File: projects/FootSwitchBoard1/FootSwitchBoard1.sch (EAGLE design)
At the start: 10 parts

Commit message: Board updates.
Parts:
- added BD_V+, BD_V/2, GND, GND1, GND2, GND3, GND4, GND5, JK_V+: WIREPAD2,54/0,8, wirepad:WIREPAD2,54/0,8
- added C2: (no value), gm-caps-film-box:072X0352
- added C3: (no value), gm-caps-electro-pol:080
- added R3, R4: (no value), gm-resistors:6MM.4
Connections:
- new net N$10: BD_V/2.P, C3.+, R3.1, R4.2
- new net N$11: C1.-, C2.2, C3.-, GND.P, GND1.P, GND2.P, GND3.P, GND4.P, GND5.P, R4.1, U$1.A1, U$1.A2, U$1.B1
- new net N$9: BD_V+.P, C1.+, C2.1, D1.A, R2.2, R3.2
- net N$7: now also D2.A, JK_V+.P; no longer U$1.A1, U$1.A2, U$1.B1
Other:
- moved on the sheet: R2
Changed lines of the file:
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@@
 <part name="R2" library="gm-resistors" deviceset="6MM" device=".4"/>
 <part name="C1" library="gm-caps-electro-pol" deviceset="080" device=""/>
+<part name="C2" library="gm-caps-film-box" deviceset="072X035" device="2"/>
+<part name="R3" library="gm-resistors" deviceset="6MM" device=".4"/>
+<part name="R4" library="gm-resistors" deviceset="6MM" device=".4"/>
+<part name="C3" library="gm-caps-electro-pol" deviceset="080" device=""/>
+<part name="JK_V+" library="wirepad" deviceset="WIREPAD" device="2,54/0,8"/>
+<part name="GND" library="wirepad" deviceset="WIREPAD" device="2,54/0,8"/>
+<part name="BD_V/2" library="wirepad" deviceset="WIREPAD" device="2,54/0,8"/>
+<part name="BD_V+" library="wirepad" deviceset="WIREPAD" device="2,54/0,8"/>
+<part name="GND1" library="wirepad" deviceset="WIREPAD" device="2,54/0,8"/>
+<part name="GND2" library="wirepad" deviceset="WIREPAD" device="2,54/0,8"/>
+<part name="GND3" library="wirepad" deviceset="WIREPAD" device="2,54/0,8"/>
+<part name="GND4" library="wirepad" deviceset="WIREPAD" device="2,54/0,8"/>
+<part name="GND5" library="wirepad" deviceset="WIREPAD" device="2,54/0,8"/>
 </parts>
 <sheets>
@@
 <instance part="R1" gate="G$1" x="93.98" y="68.58"/>
 <instance part="D2" gate="1" x="17.78" y="81.28"/>
-<instance part="R2" gate="G$1" x="35.56" y="81.28"/>
+<instance part="R2" gate="G$1" x="30.48" y="81.28"/>
 <instance part="C1" gate="G$1" x="45.72" y="78.74"/>
+<instance part="C2" gate="G$1" x="53.34" y="76.2"/>
+<instance part="R3" gate="G$1" x="30.48" y="66.04" rot="R90"/>
+<instance part="R4" gate="G$1" x="30.48" y="50.8" rot="R90"/>
+<instance part="C3" gate="G$1" x="22.86" y="53.34"/>
+<instance part="JK_V+" gate="G$1" x="2.54" y="81.28"/>
+<instance part="GND" gate="G$1" x="5.08" y="45.72"/>
+<instance part="BD_V/2" gate="G$1" x="15.24" y="55.88"/>
+<instance part="BD_V+" gate="G$1" x="15.24" y="71.12"/>
+<instance part="GND1" gate="G$1" x="5.08" y="38.1"/>
+<instance part="GND2" gate="G$1" x="5.08" y="30.48"/>
+<instance part="GND3" gate="G$1" x="5.08" y="22.86"/>
+<instance part="GND4" gate="G$1" x="5.08" y="15.24"/>
+<instance part="GND5" gate="G$1" x="5.08" y="7.62"/>
 </instances>
 <busses>
@@
 </segment>
 </net>
-<net name="N$7" class="0">
-<segment>
+<net name="N$8" class="0">
+<segment>
+<pinref part="D2" gate="1" pin="C"/>
+<wire x1="20.32" y1="81.28" x2="25.4" y2="81.28" width="0.1524" layer="91"/>
+<pinref part="R2" gate="G$1" pin="1"/>
+</segment>
+</net>
+<net name="N$9" class="0">
+<segment>
+<pinref part="R2" gate="G$1" pin="2"/>
+<pinref part="C1" gate="G$1" pin="+"/>
+<wire x1="35.56" y1="81.28" x2="45.72" y2="81.28" width="0.1524" layer="91"/>
+<pinref part="C2" gate="G$1" pin="1"/>
+<wire x1="45.72" y1="81.28" x2="53.34" y2="81.28" width="0.1524" layer="91"/>
+<junction x="45.72" y="81.28"/>
+<wire x1="35.56" y1="81.28" x2="35.56" y2="73.66" width="0.1524" layer="91"/>
+<junction x="35.56" y="81.28"/>
+<pinref part="R3" gate="G$1" pin="2"/>
+<wire x1="35.56" y1="73.66" x2="30.48" y2="73.66" width="0.1524" layer="91"/>
+<wire x1="30.48" y1="73.66" x2="30.48" y2="71.12" width="0.1524" layer="91"/>
+<pinref part="D1" gate="G$1" pin="A"/>
+<wire x1="119.38" y1="68.58" x2="119.38" y2="78.74" width="0.1524" layer="91"/>
+<wire x1="119.38" y1="78.74" x2="60.96" y2="78.74" width="0.1524" layer="91"/>
+<wire x1="60.96" y1="78.74" x2="60.96" y2="81.28" width="0.1524" layer="91"/>
+<wire x1="60.96" y1="81.28" x2="53.34" y2="81.28" width="0.1524" layer="91"/>
+<junction x="53.34" y="81.28"/>
+<pinref part="BD_V+" gate="G$1" pin="P"/>
+<wire x1="17.78" y1="71.12" x2="25.4" y2="71.12" width="0.1524" layer="91"/>
+<wire x1="25.4" y1="71.12" x2="25.4" y2="73.66" width="0.1524" layer="91"/>
+<wire x1="25.4" y1="73.66" x2="30.48" y2="73.66" width="0.1524" layer="91"/>
+<junction x="30.48" y="73.66"/>
+</segment>
+</net>
+<net name="N$10" class="0">
+<segment>
+<pinref part="R3" gate="G$1" pin="1"/>
+<pinref part="R4" gate="G$1" pin="2"/>
+<wire x1="30.48" y1="60.96" x2="30.48" y2="55.88" width="0.1524" layer="91"/>
+<pinref part="C3" gate="G$1" pin="+"/>
+<wire x1="22.86" y1="55.88" x2="30.48" y2="55.88" width="0.1524" layer="91"/>
+<junction x="30.48" y="55.88"/>
+<pinref part="BD_V/2" gate="G$1" pin="P"/>
+<wire x1="17.78" y1="55.88" x2="22.86" y2="55.88" width="0.1524" layer="91"/>
+<junction x="22.86" y="55.88"/>
+</segment>
+</net>
+<net name="N$11" class="0">
+<segment>
+<pinref part="C3" gate="G$1" pin="-"/>
+<wire x1="22.86" y1="48.26" x2="22.86" y2="45.72" width="0.1524" layer="91"/>
+<pinref part="R4" gate="G$1" pin="1"/>
+<wire x1="22.86" y1="45.72" x2="30.48" y2="45.72" width="0.1524" layer="91"/>
+<wire x1="30.48" y1="45.72" x2="43.18" y2="45.72" width="0.1524" layer="91"/>
+<wire x1="43.18" y1="45.72" x2="43.18" y2="73.66" width="0.1524" layer="91"/>
+<junction x="30.48" y="45.72"/>
+<pinref part="C1" gate="G$1" pin="-"/>
+<wire x1="43.18" y1="73.66" x2="45.72" y2="73.66" width="0.1524" layer="91"/>
+<pinref part="C2" gate="G$1" pin="2"/>
+<wire x1="45.72" y1="73.66" x2="53.34" y2="73.66" width="0.1524" layer="91"/>
+<junction x="45.72" y="73.66"/>
 <pinref part="U$1" gate="G$1" pin="A2"/>
 <wire x1="60.96" y1="55.88" x2="60.96" y2="60.96" width="0.1524" layer="91"/>
@@
 <wire x1="48.26" y1="50.8" x2="48.26" y2="55.88" width="0.1524" layer="91"/>
 <junction x="48.26" y="55.88"/>
-</segment>
-</net>
-<net name="N$8" class="0">
-<segment>
-<pinref part="D2" gate="1" pin="C"/>
-<wire x1="20.32" y1="81.28" x2="30.48" y2="81.28" width="0.1524" layer="91"/>
-<pinref part="R2" gate="G$1" pin="1"/>
-</segment>
-</net>
+<wire x1="45.72" y1="73.66" x2="48.26" y2="73.66" width="0.1524" layer="91"/>
+<wire x1="48.26" y1="73.66" x2="48.26" y2="60.96" width="0.1524" layer="91"/>
+<junction x="48.26" y="60.96"/>
+<pinref part="GND" gate="G$1" pin="P"/>
+<wire x1="7.62" y1="45.72" x2="22.86" y2="45.72" width="0.1524" layer="91"/>
+<junction x="22.86" y="45.72"/>
+<pinref part="GND1" gate="G$1" pin="P"/>
+<wire x1="7.62" y1="38.1" x2="22.86" y2="38.1" width="0.1524" layer="91"/>
+<wire x1="22.86" y1="38.1" x2="22.86" y2="45.72" width="0.1524" layer="91"/>
+<pinref part="GND2" gate="G$1" pin="P"/>
+<wire x1="7.62" y1="30.48" x2="22.86" y2="30.48" width="0.1524" layer="91"/>
+<wire x1="22.86" y1="30.48" x2="22.86" y2="38.1" width="0.1524" layer="91"/>
+<junction x="22.86" y="38.1"/>
+<pinref part="GND3" gate="G$1" pin="P"/>
+<wire x1="7.62" y1="22.86" x2="22.86" y2="22.86" width="0.1524" layer="91"/>
+<wire x1="22.86" y1="22.86" x2="22.86" y2="30.48" width="0.1524" layer="91"/>
+<junction x="22.86" y="30.48"/>
+<pinref part="GND4" gate="G$1" pin="P"/>
+<wire x1="7.62" y1="15.24" x2="22.86" y2="15.24" width="0.1524" layer="91"/>
+<wire x1="22.86" y1="15.24" x2="22.86" y2="22.86" width="0.1524" layer="91"/>
+<junction x="22.86" y="22.86"/>
+<pinref part="GND5" gate="G$1" pin="P"/>
+<wire x1="7.62" y1="7.62" x2="22.86" y2="7.62" width="0.1524" layer="91"/>
+<wire x1="22.86" y1="7.62" x2="22.86" y2="15.24" width="0.1524" layer="91"/>
+<junction x="22.86" y="15.24"/>
+</segment>
+</net>
+<net name="N$7" class="0">
+<segment>
+<pinref part="JK_V+" gate="G$1" pin="P"/>
+<pinref part="D2" gate="1" pin="A"/>
+<wire x1="5.08" y1="81.28" x2="12.7" y2="81.28" width="0.1524" layer="91"/>
+</segment>
+</net>

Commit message: Board layout in progress.
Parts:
- removed BD_IN, BD_OUT, BD_V+, BD_V/2, GND, GND1, GND2, GND3, GND4, GND5, JK_IN, JK_OUT, JK_V+: WIREPAD2,54/0,8, wirepad:WIREPAD2,54/0,8
- added -9, 18, 9IN1, 9IN2, BDI, BDO, BDO1, BDV, G0, G1, G2, G3, G4, G5, G6, GD, GN, JKI, JKO, V/2, VIN: WIREPAD2,15/1,0, wirepad:WIREPAD2,15/1,0
- added C4, C5, C6, C7: 10u, gm-caps-electro-pol:050
- added D3: (no value), gm-diodes:1N9ZENER
- added D5, D6: (no value), gm-diodes:1N400X.3
- added R5: (no value), gm-resistors:10MM
- added TC1044S, TC1044S1: (no value), ic-package:DIL8S
- R1, R2, R3, R4: device gm-resistors:6MM.4 -> gm-resistors:6MM.3
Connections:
- new net -9GND: C7.+, GN.P, TC1044S1.3
- new net 18VGND: C4.-, C5.-, GD.P, TC1044S.3, TC1044S.5
- new net N$12: D3.A, R5.2
- new net N$13: 9IN2.P, D5.A, TC1044S.1, TC1044S.8
- new net N$14: C4.+, D5.C, D6.A
- new net N$15: 18.P, C5.+, D6.C
- new net N$16: 9IN1.P, TC1044S1.1, TC1044S1.8
- new net N$17: -9.P, C7.-, TC1044S1.5
- new net N$20: C6.+, TC1044S1.2
- new net N$21: C6.-, TC1044S1.4
- net N$1: now also JKI.P; no longer JK_IN.P
- net N$10: now also V/2.P; no longer BD_V/2.P
- net N$11: now also G0.P, G1.P, G2.P, G3.P, G4.P, G5.P, G6.P, R5.1; no longer GND.P, GND1.P, GND2.P, GND3.P, GND4.P, GND5.P
- net N$2: now also JKO.P; no longer JK_OUT.P
- net N$3: now also BDO.P, BDO1.P; no longer BD_OUT.P
- net N$4: now also BDI.P; no longer BD_IN.P
- net N$7: now also VIN.P; no longer JK_V+.P
- net N$9: now also BDV.P, D3.C; no longer BD_V+.P

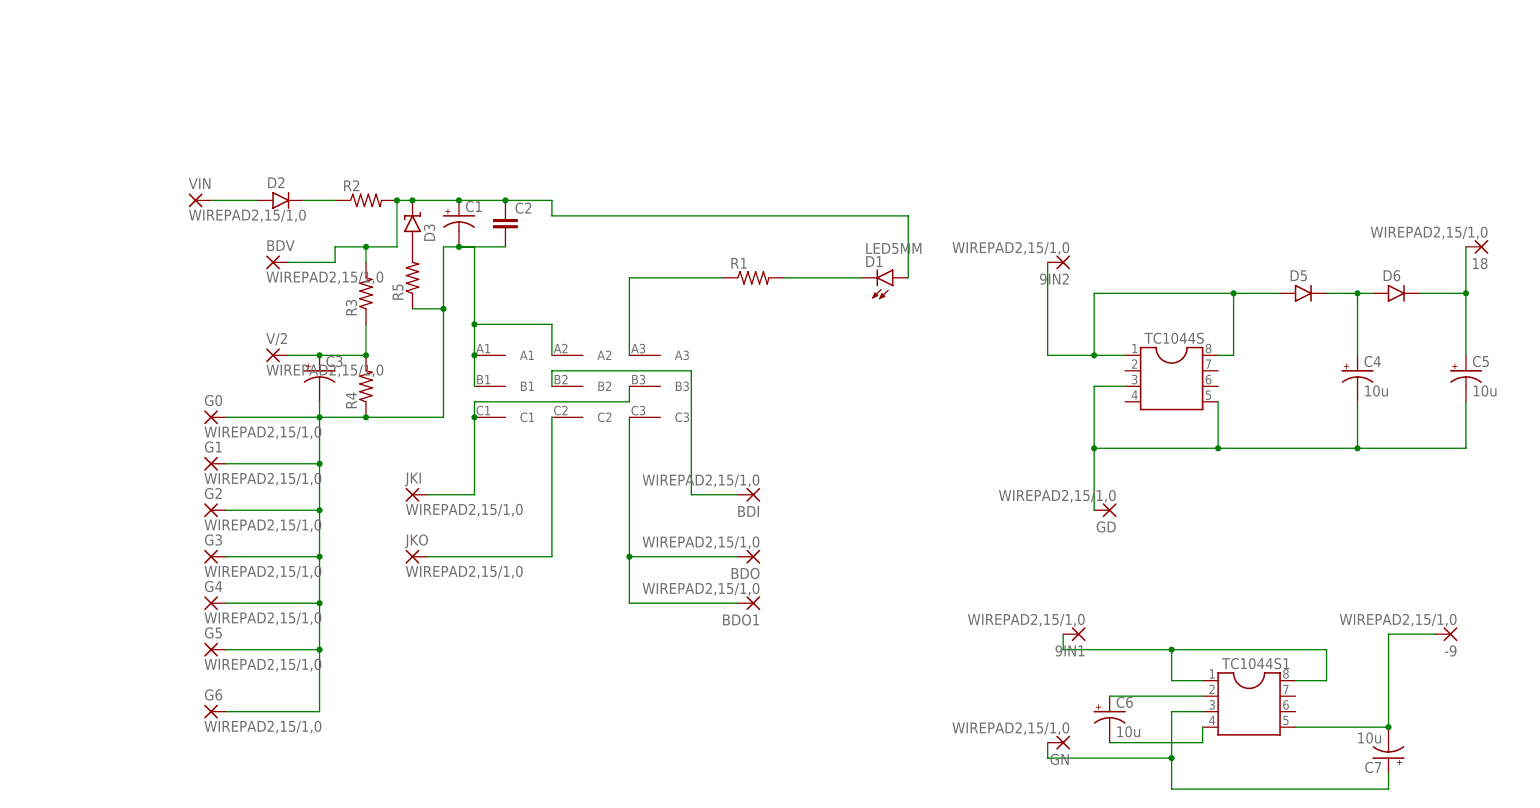
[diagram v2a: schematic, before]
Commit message: Implemented combined inverter/doubler board.
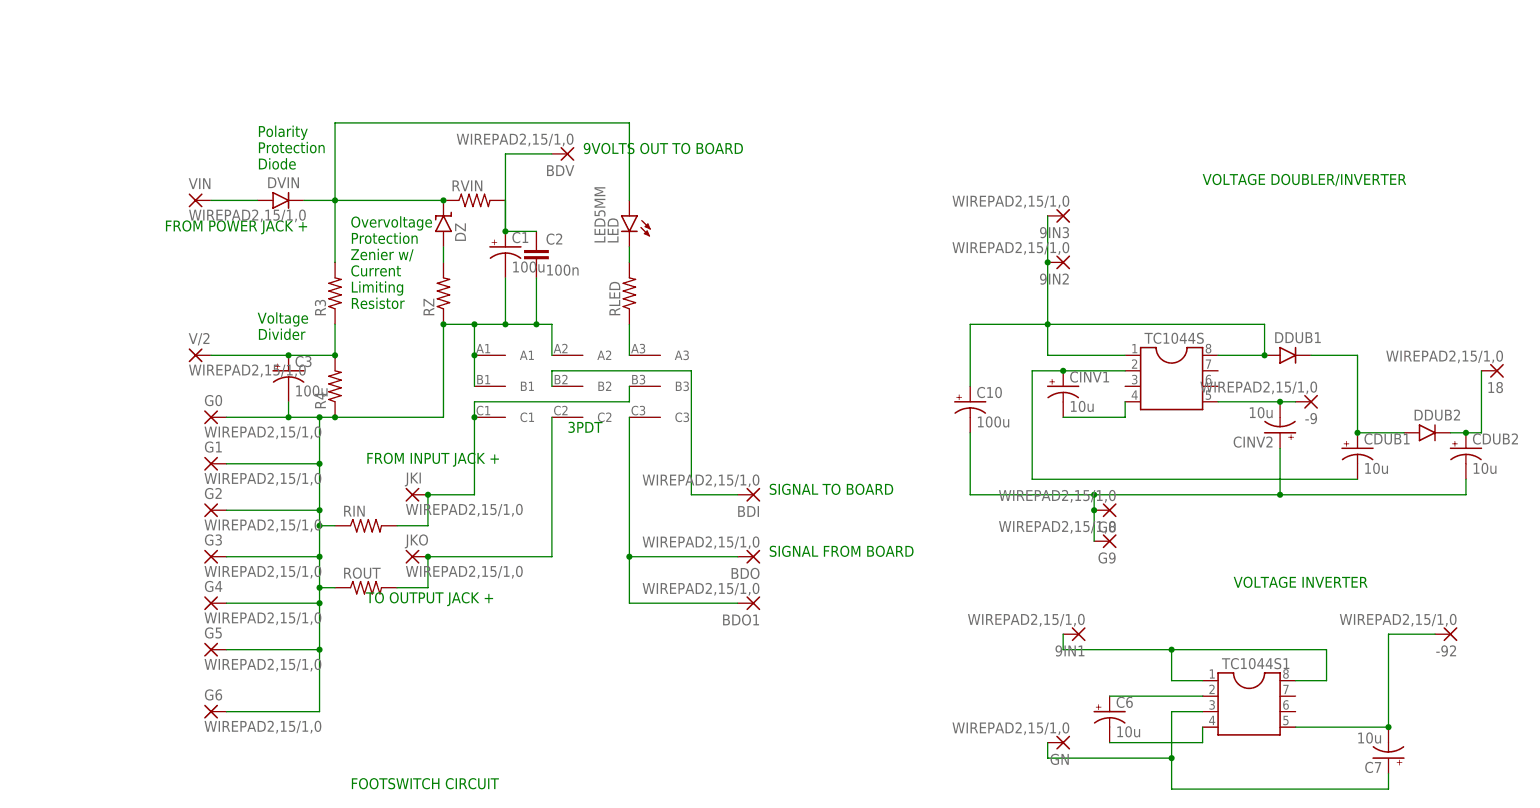
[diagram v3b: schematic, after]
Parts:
- removed C4, C5: 10u, gm-caps-electro-pol:050
- removed D1: LED5MM, gm-diodes:LED5MM
- removed D3: (no value), gm-diodes:1N9ZENER
- removed D5, D6: (no value), gm-diodes:1N400X.3
- removed R1, R2: (no value), gm-resistors:6MM.3
- removed R5: (no value), gm-resistors:10MM
- added -92, 9IN3, G9: WIREPAD2,15/1,0, wirepad:WIREPAD2,15/1,0
- added C10: 100u, gm-caps-electro-pol:080
- added CDUB1, CDUB2, CINV1, CINV2: 10u, gm-caps-electro-pol:050
- added DDUB1, DDUB2: (no value), gm-diodes:1N400X.3
- added DZ: (no value), gm-diodes:1N9ZENER
- added LED: LED5MM, gm-diodes:LED5MM
- added RIN, RLED, ROUT, RVIN: (no value), gm-resistors:6MM.3
- added RZ: (no value), gm-resistors:10MM
- C1, C3: value (none) -> 100u
- C2: value (none) -> 100n
- renumbered D2 to DVIN, GD to G8
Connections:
- removed net 18VGND: C4.-, C5.-, G8.P, TC1044S.3, TC1044S.5
- removed net N$14: C4.+, D5.C, D6.A
- removed net N$9: BDV.P, C1.+, C2.1, D1.A, D3.C, R2.2, R3.2
- new net 9INDUBINV: 9IN2.P, 9IN3.P, C10.+, DDUB1.A, TC1044S.1, TC1044S.8
- new net DDUB2: CDUB1.+, DDUB1.C, DDUB2.A
- new net GDUBINV: C10.-, CDUB2.-, CINV2.+, G8.P, G9.P
- new net N$18: DVIN.C, DZ.C, LED.A, R3.2, RVIN.1
- new net N$19: -9.P, CINV2.-, TC1044S.5
- new net N$22: 18.P, CDUB2.+, DDUB2.C
- net N$1: now also RIN.2
- net N$11: now also RIN.1, ROUT.1, RZ.1; no longer R5.1
- net N$12: now also DZ.A, RZ.2; no longer D3.A, R5.2
- net N$13: now also CDUB1.-, CINV1.+, TC1044S.2; no longer 9IN2.P, D5.A, TC1044S.1, TC1044S.8
- net N$15: now also CINV1.-, TC1044S.4; no longer 18.P, C5.+, D6.C
- net N$17: now also -92.P; no longer -9.P
- net N$2: now also ROUT.2
- net N$5: now also LED.C, RLED.2; no longer D1.C, R1.2
- net N$6: now also RLED.1; no longer R1.1
- net N$8: now also BDV.P, C1.+, C2.1, RVIN.2; no longer DVIN.C, R2.1
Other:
- note added: "3PDT"
- note added: "9VOLTS OUT TO BOARD"
- note added: "FOOTSWITCH CIRCUIT"
- note added: "FROM INPUT JACK +"
- note added: "FROM POWER JACK +"
- note added: "Overvoltage Protection Zenier w/ Current Limiting Resistor"
- note added: "Polarity Protection Diode"
- note added: "SIGNAL FROM BOARD"
- note added: "SIGNAL TO BOARD"
- note added: "TO OUTPUT JACK +"
- note added: "VOLTAGE DOUBLER/INVERTER"
- note added: "VOLTAGE INVERTER"
- note added: "Voltage Divider"
- moved on the sheet: -9, 18, BDV, C1, C2, C3, R3, R4, V/2

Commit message: Circuit mods, new OVP UVP circuit added.
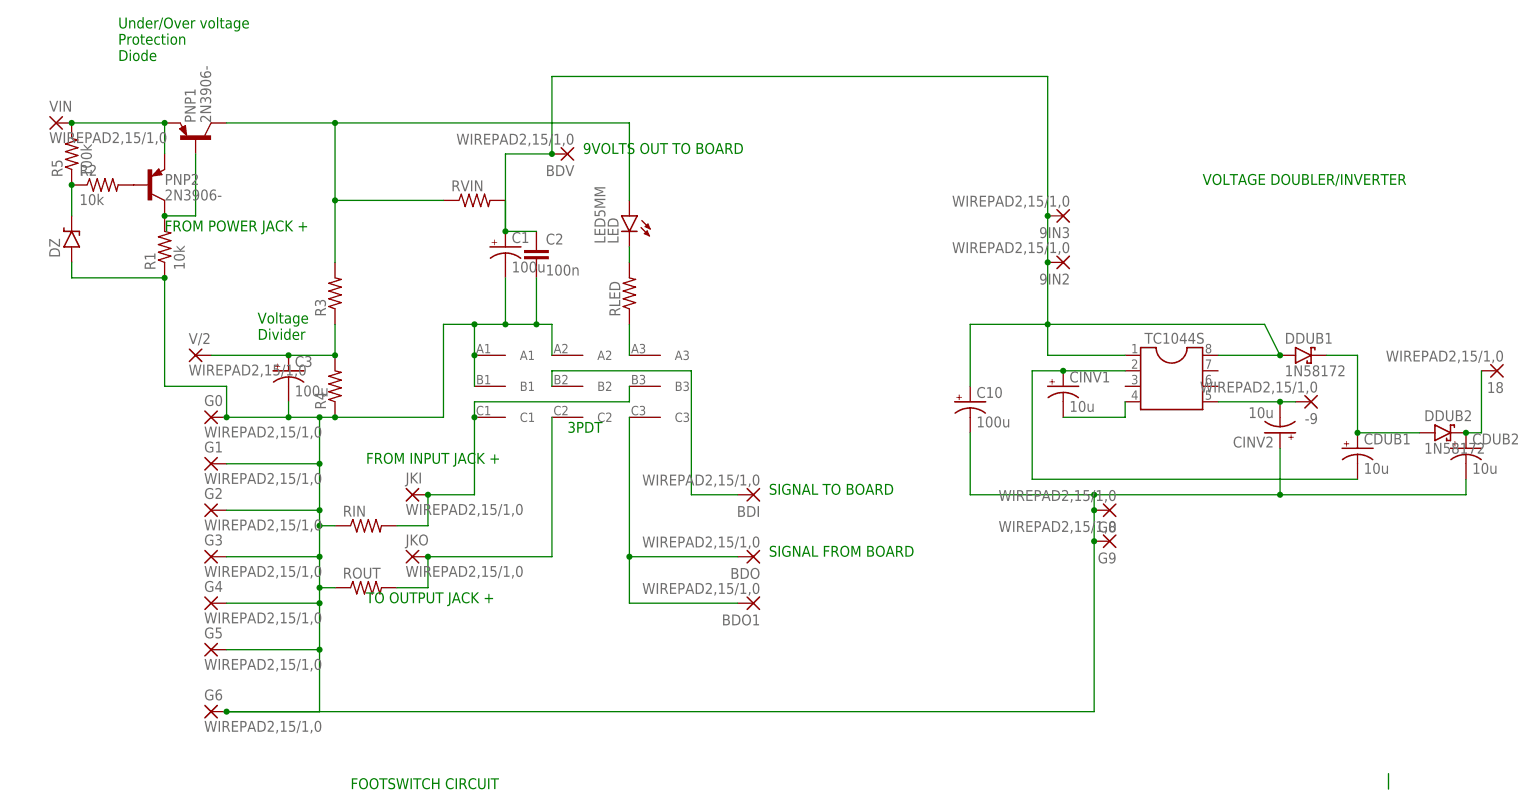
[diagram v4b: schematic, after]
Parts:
- removed -92, 9IN1, GN: WIREPAD2,15/1,0, wirepad:WIREPAD2,15/1,0
- removed C6, C7: 10u, gm-caps-electro-pol:050
- removed DVIN: (no value), gm-diodes:1N400X.3
- removed RZ: (no value), gm-resistors:10MM
- removed TC1044S1: (no value), ic-package:DIL8S
- added PNP1, PNP2: 2N3906-, gm-trans:2N3906-
- added R1, R2: 10k, gm-resistors:6MM.2
- added R5: 100k, gm-resistors:6MM.2
- DDUB1, DDUB2: value (none) -> 1N58172; device gm-diodes:1N400X.3 -> gm-diodes:1N58172
- DZ: device gm-diodes:1N9ZENER -> gm-diodes:1N47XX2
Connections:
- removed net -9GND: C7.+, GN.P, TC1044S1.3
- removed net N$11: C1.-, C2.2, C3.-, G0.P, G1.P, G2.P, G3.P, G4.P, G5.P, G6.P, R4.1, RIN.1, ROUT.1, RZ.1, U$1.A1, U$1.A2, U$1.B1
- removed net N$12: DZ.A, RZ.2
- removed net N$16: 9IN1.P, TC1044S1.1, TC1044S1.8
- removed net N$17: -92.P, C7.-, TC1044S1.5
- removed net N$18: DVIN.C, DZ.C, LED.A, R3.2, RVIN.1
- removed net N$20: C6.+, TC1044S1.2
- removed net N$21: C6.-, TC1044S1.4
- removed net N$7: DVIN.A, VIN.P
- removed net N$8: BDV.P, C1.+, C2.1, RVIN.2
- new net N$14: DZ.C, R2.1, R5.1
- new net N$23: PNP1.B, PNP2.C, R1.2
- new net N$24: PNP1.E, PNP2.E, R5.2, VIN.P
- new net N$25: LED.A, PNP1.C, R3.2, RVIN.1
- new net N$9: PNP2.B, R2.2
- net 9INDUBINV: now also BDV.P, C1.+, C2.1, RVIN.2
- net GDUBINV: now also C1.-, C2.2, C3.-, DZ.A, G0.P, G1.P, G2.P, G3.P, G4.P, G5.P, G6.P, R1.1, R4.1, RIN.1, ROUT.1, U$1.A1, U$1.A2, U$1.B1
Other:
- note added: "Under/Over voltage Protection Diode"
- note removed: "Overvoltage Protection Zenier w/ Current Limiting Resistor"
- note removed: "Polarity Protection Diode"
- note removed: "VOLTAGE INVERTER"
- moved on the sheet: VIN
